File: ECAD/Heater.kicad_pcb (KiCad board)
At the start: 2 copper layers, 200 x 200 mm, 11 parts, among them J1 Conn_01x01_Female, J2 Conn_01x01_Female

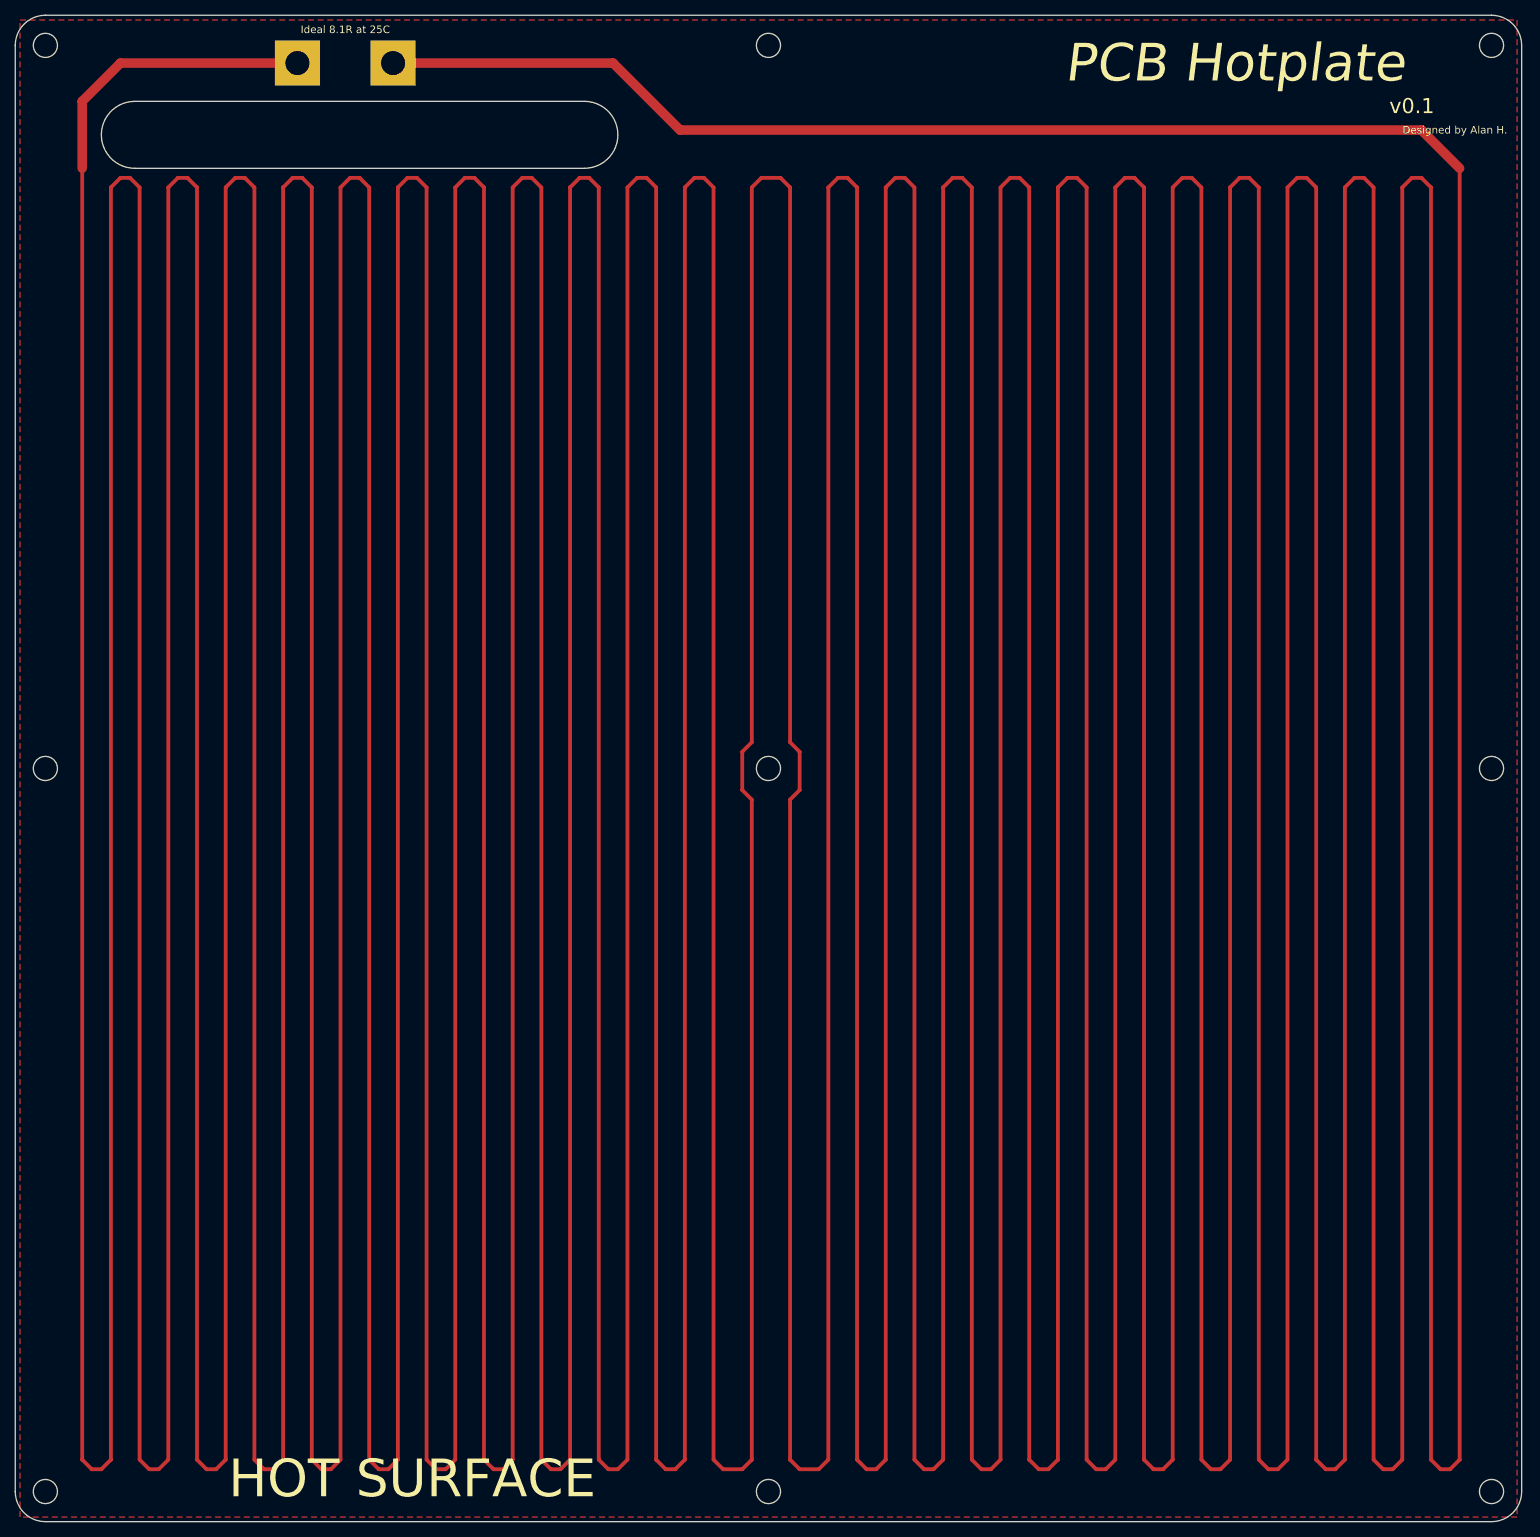
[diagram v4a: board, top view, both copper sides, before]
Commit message: Revert "Merge pull request #3 from Alan-JH/revert-2-Perforated-Heater"
This reverts commit 4dedab5329d0c4c589ebeff6f2ce44676f29a142, reversing
changes made to 18337d37710a704d8d57a7691b9b75f48685949f.
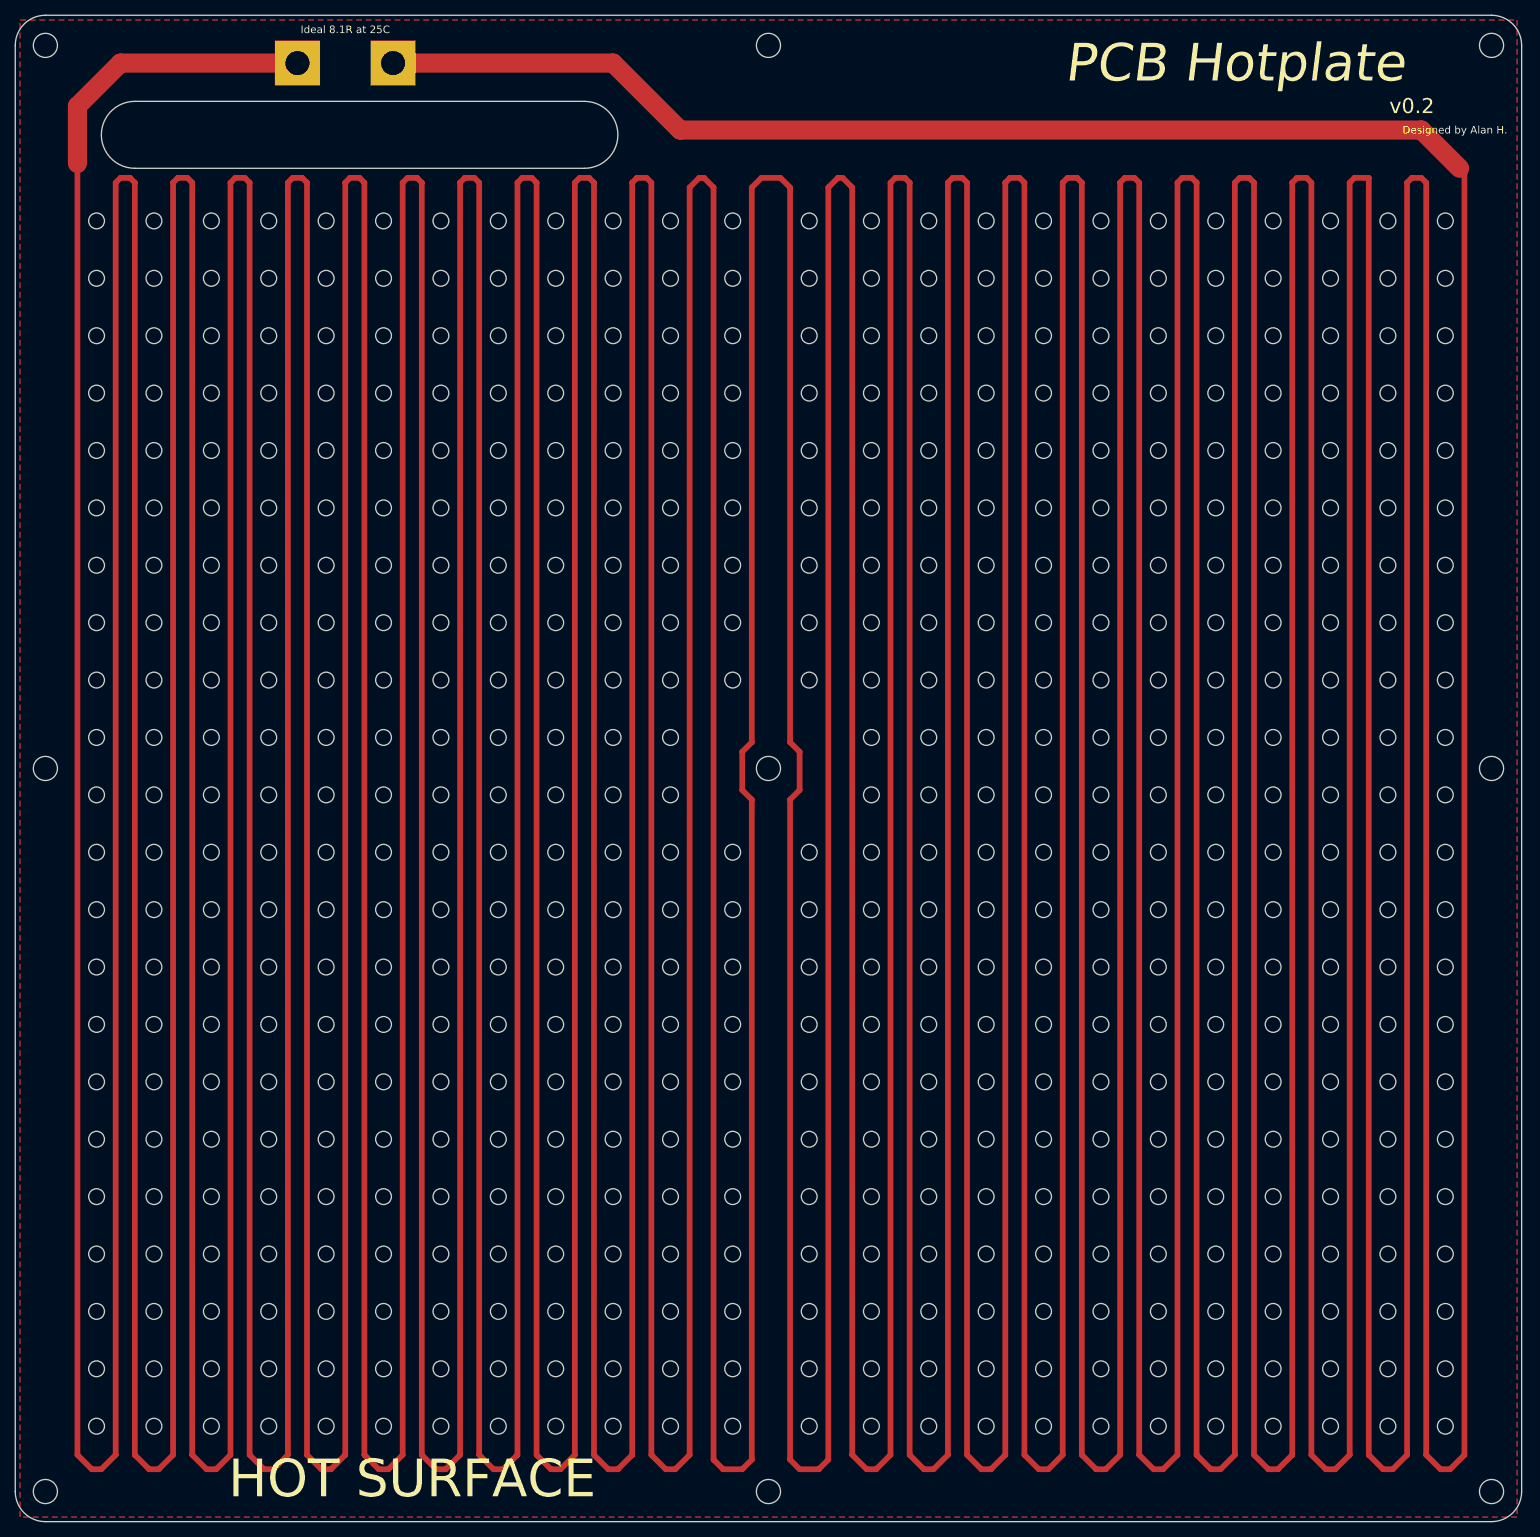
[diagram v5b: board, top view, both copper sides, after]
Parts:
- added REF**: MountingHole_2.1mm, MountingHole:MountingHole_2.1mm, F.Cu at (97.2, 37.5)
- added REF**: MountingHole_2.1mm, MountingHole:MountingHole_2.1mm, F.Cu at (81.9, 37.5)
- added REF**: MountingHole_2.1mm, MountingHole:MountingHole_2.1mm, F.Cu at (146.7, 67.9)
- added REF**: MountingHole_2.1mm, MountingHole:MountingHole_2.1mm, F.Cu at (89.5, 67.9)
- added REF**: MountingHole_2.1mm, MountingHole:MountingHole_2.1mm, F.Cu at (139.1, 67.9)
- added REF**: MountingHole_2.1mm, MountingHole:MountingHole_2.1mm, F.Cu at (123.8, 67.9)
- added REF**: MountingHole_2.1mm, MountingHole:MountingHole_2.1mm, F.Cu at (105.4, 67.9)
- added REF**: MountingHole_2.1mm, MountingHole:MountingHole_2.1mm, F.Cu at (115.6, 67.9)
- added REF**: MountingHole_2.1mm, MountingHole:MountingHole_2.1mm, F.Cu at (81.9, 67.9)
- added REF**: MountingHole_2.1mm, MountingHole:MountingHole_2.1mm, F.Cu at (74.3, 67.9)
- added REF**: MountingHole_2.1mm, MountingHole:MountingHole_2.1mm, F.Cu at (66.7, 67.9)
- added REF**: MountingHole_2.1mm, MountingHole:MountingHole_2.1mm, F.Cu at (51.4, 67.9)
- added REF**: MountingHole_2.1mm, MountingHole:MountingHole_2.1mm, F.Cu at (74.3, 37.5)
- added REF**: MountingHole_2.1mm, MountingHole:MountingHole_2.1mm, F.Cu at (59.1, 67.9)
- added REF**: MountingHole_2.1mm, MountingHole:MountingHole_2.1mm, F.Cu at (43.8, 67.9)
- added REF**: MountingHole_2.1mm, MountingHole:MountingHole_2.1mm, F.Cu at (28.6, 67.9)
- added REF**: MountingHole_2.1mm, MountingHole:MountingHole_2.1mm, F.Cu at (21.0, 67.9)
- added REF**: MountingHole_2.1mm, MountingHole:MountingHole_2.1mm, F.Cu at (200.0, 75.6)
- added REF**: MountingHole_2.1mm, MountingHole:MountingHole_2.1mm, F.Cu at (192.4, 75.6)
- added REF**: MountingHole_2.1mm, MountingHole:MountingHole_2.1mm, F.Cu at (184.8, 75.6)
- added REF**: MountingHole_2.1mm, MountingHole:MountingHole_2.1mm, F.Cu at (177.2, 75.6)
- added REF**: MountingHole_2.1mm, MountingHole:MountingHole_2.1mm, F.Cu at (169.5, 75.6)
- added REF**: MountingHole_2.1mm, MountingHole:MountingHole_2.1mm, F.Cu at (146.7, 75.6)
- added REF**: MountingHole_2.1mm, MountingHole:MountingHole_2.1mm, F.Cu at (66.7, 37.5)
- added REF**: MountingHole_2.1mm, MountingHole:MountingHole_2.1mm, F.Cu at (161.9, 75.6)
- added REF**: MountingHole_2.1mm, MountingHole:MountingHole_2.1mm, F.Cu at (154.3, 75.6)
- added REF**: MountingHole_2.1mm, MountingHole:MountingHole_2.1mm, F.Cu at (139.1, 75.6)
- added REF**: MountingHole_2.1mm, MountingHole:MountingHole_2.1mm, F.Cu at (131.4, 75.6)
- added REF**: MountingHole_2.1mm, MountingHole:MountingHole_2.1mm, F.Cu at (123.8, 75.6)
- added REF**: MountingHole_2.1mm, MountingHole:MountingHole_2.1mm, F.Cu at (115.6, 75.6)
- added REF**: MountingHole_2.1mm, MountingHole:MountingHole_2.1mm, F.Cu at (105.4, 75.6)
- added REF**: MountingHole_2.1mm, MountingHole:MountingHole_2.1mm, F.Cu at (97.2, 75.6)
- added REF**: MountingHole_2.1mm, MountingHole:MountingHole_2.1mm, F.Cu at (89.5, 75.6)
- added REF**: MountingHole_2.1mm, MountingHole:MountingHole_2.1mm, F.Cu at (51.4, 75.6)
- added REF**: MountingHole_2.1mm, MountingHole:MountingHole_2.1mm, F.Cu at (51.4, 37.5)
- added REF**: MountingHole_2.1mm, MountingHole:MountingHole_2.1mm, F.Cu at (43.8, 75.6)
- added REF**: MountingHole_2.1mm, MountingHole:MountingHole_2.1mm, F.Cu at (36.2, 75.6)
- added REF**: MountingHole_2.1mm, MountingHole:MountingHole_2.1mm, F.Cu at (36.2, 67.9)
- added REF**: MountingHole_2.1mm, MountingHole:MountingHole_2.1mm, F.Cu at (66.7, 75.6)
- added REF**: MountingHole_2.1mm, MountingHole:MountingHole_2.1mm, F.Cu at (81.9, 75.6)
- added REF**: MountingHole_2.1mm, MountingHole:MountingHole_2.1mm, F.Cu at (59.1, 75.6)
- added REF**: MountingHole_2.1mm, MountingHole:MountingHole_2.1mm, F.Cu at (74.3, 75.6)
- added REF**: MountingHole_2.1mm, MountingHole:MountingHole_2.1mm, F.Cu at (28.6, 75.6)
- added REF**: MountingHole_2.1mm, MountingHole:MountingHole_2.1mm, F.Cu at (21.0, 75.6)
- added REF**: MountingHole_2.1mm, MountingHole:MountingHole_2.1mm, F.Cu at (192.4, 67.9)
- added REF**: MountingHole_2.1mm, MountingHole:MountingHole_2.1mm, F.Cu at (59.1, 37.5)
- added REF**: MountingHole_2.1mm, MountingHole:MountingHole_2.1mm, F.Cu at (161.9, 67.9)
- added REF**: MountingHole_2.1mm, MountingHole:MountingHole_2.1mm, F.Cu at (169.5, 67.9)
- added REF**: MountingHole_2.1mm, MountingHole:MountingHole_2.1mm, F.Cu at (184.8, 67.9)
- added REF**: MountingHole_2.1mm, MountingHole:MountingHole_2.1mm, F.Cu at (200.0, 67.9)
- added REF**: MountingHole_2.1mm, MountingHole:MountingHole_2.1mm, F.Cu at (177.2, 67.9)
- added REF**: MountingHole_2.1mm, MountingHole:MountingHole_2.1mm, F.Cu at (97.2, 83.2)
- added REF**: MountingHole_2.1mm, MountingHole:MountingHole_2.1mm, F.Cu at (131.4, 83.2)
- added REF**: MountingHole_2.1mm, MountingHole:MountingHole_2.1mm, F.Cu at (154.3, 83.2)
- added REF**: MountingHole_2.1mm, MountingHole:MountingHole_2.1mm, F.Cu at (146.7, 83.2)
- added REF**: MountingHole_2.1mm, MountingHole:MountingHole_2.1mm, F.Cu at (89.5, 83.2)
- added REF**: MountingHole_2.1mm, MountingHole:MountingHole_2.1mm, F.Cu at (43.8, 37.5)
- added REF**: MountingHole_2.1mm, MountingHole:MountingHole_2.1mm, F.Cu at (139.1, 83.2)
- added REF**: MountingHole_2.1mm, MountingHole:MountingHole_2.1mm, F.Cu at (123.8, 83.2)
- added REF**: MountingHole_2.1mm, MountingHole:MountingHole_2.1mm, F.Cu at (105.4, 83.2)
- added REF**: MountingHole_2.1mm, MountingHole:MountingHole_2.1mm, F.Cu at (115.6, 83.2)
- added REF**: MountingHole_2.1mm, MountingHole:MountingHole_2.1mm, F.Cu at (81.9, 83.2)
- added REF**: MountingHole_2.1mm, MountingHole:MountingHole_2.1mm, F.Cu at (74.3, 83.2)
- added REF**: MountingHole_2.1mm, MountingHole:MountingHole_2.1mm, F.Cu at (66.7, 83.2)
- added REF**: MountingHole_2.1mm, MountingHole:MountingHole_2.1mm, F.Cu at (51.4, 83.2)
- added REF**: MountingHole_2.1mm, MountingHole:MountingHole_2.1mm, F.Cu at (59.1, 83.2)
- added REF**: MountingHole_2.1mm, MountingHole:MountingHole_2.1mm, F.Cu at (43.8, 83.2)
- added REF**: MountingHole_2.1mm, MountingHole:MountingHole_2.1mm, F.Cu at (28.6, 37.5)
- added REF**: MountingHole_2.1mm, MountingHole:MountingHole_2.1mm, F.Cu at (28.6, 83.2)
- added REF**: MountingHole_2.1mm, MountingHole:MountingHole_2.1mm, F.Cu at (21.0, 83.2)
- added REF**: MountingHole_2.1mm, MountingHole:MountingHole_2.1mm, F.Cu at (200.0, 90.8)
- added REF**: MountingHole_2.1mm, MountingHole:MountingHole_2.1mm, F.Cu at (192.4, 90.8)
- added REF**: MountingHole_2.1mm, MountingHole:MountingHole_2.1mm, F.Cu at (184.8, 90.8)
- added REF**: MountingHole_2.1mm, MountingHole:MountingHole_2.1mm, F.Cu at (177.2, 90.8)
- added REF**: MountingHole_2.1mm, MountingHole:MountingHole_2.1mm, F.Cu at (169.5, 90.8)
- added REF**: MountingHole_2.1mm, MountingHole:MountingHole_2.1mm, F.Cu at (146.7, 90.8)
- added REF**: MountingHole_2.1mm, MountingHole:MountingHole_2.1mm, F.Cu at (161.9, 90.8)
- added REF**: MountingHole_2.1mm, MountingHole:MountingHole_2.1mm, F.Cu at (154.3, 90.8)
- added REF**: MountingHole_2.1mm, MountingHole:MountingHole_2.1mm, F.Cu at (21.0, 37.5)
- added REF**: MountingHole_2.1mm, MountingHole:MountingHole_2.1mm, F.Cu at (139.1, 90.8)
- added REF**: MountingHole_2.1mm, MountingHole:MountingHole_2.1mm, F.Cu at (131.4, 90.8)
- added REF**: MountingHole_2.1mm, MountingHole:MountingHole_2.1mm, F.Cu at (123.8, 90.8)
- added REF**: MountingHole_2.1mm, MountingHole:MountingHole_2.1mm, F.Cu at (115.6, 90.8)
- added REF**: MountingHole_2.1mm, MountingHole:MountingHole_2.1mm, F.Cu at (105.4, 90.8)
- added REF**: MountingHole_2.1mm, MountingHole:MountingHole_2.1mm, F.Cu at (97.2, 90.8)
- added REF**: MountingHole_2.1mm, MountingHole:MountingHole_2.1mm, F.Cu at (89.5, 90.8)
- added REF**: MountingHole_2.1mm, MountingHole:MountingHole_2.1mm, F.Cu at (51.4, 90.8)
- added REF**: MountingHole_2.1mm, MountingHole:MountingHole_2.1mm, F.Cu at (43.8, 90.8)
- added REF**: MountingHole_2.1mm, MountingHole:MountingHole_2.1mm, F.Cu at (36.2, 90.8)
- added REF**: MountingHole_2.1mm, MountingHole:MountingHole_2.1mm, F.Cu at (200.0, 45.1)
- added REF**: MountingHole_2.1mm, MountingHole:MountingHole_2.1mm, F.Cu at (36.2, 83.2)
- added REF**: MountingHole_2.1mm, MountingHole:MountingHole_2.1mm, F.Cu at (66.7, 90.8)
- added REF**: MountingHole_2.1mm, MountingHole:MountingHole_2.1mm, F.Cu at (81.9, 90.8)
- added REF**: MountingHole_2.1mm, MountingHole:MountingHole_2.1mm, F.Cu at (59.1, 90.8)
- added REF**: MountingHole_2.1mm, MountingHole:MountingHole_2.1mm, F.Cu at (74.3, 90.8)
- added REF**: MountingHole_2.1mm, MountingHole:MountingHole_2.1mm, F.Cu at (28.6, 90.8)
- added REF**: MountingHole_2.1mm, MountingHole:MountingHole_2.1mm, F.Cu at (21.0, 90.8)
- added REF**: MountingHole_2.1mm, MountingHole:MountingHole_2.1mm, F.Cu at (192.4, 83.2)
- added REF**: MountingHole_2.1mm, MountingHole:MountingHole_2.1mm, F.Cu at (161.9, 83.2)
- added REF**: MountingHole_2.1mm, MountingHole:MountingHole_2.1mm, F.Cu at (169.5, 83.2)
- added REF**: MountingHole_2.1mm, MountingHole:MountingHole_2.1mm, F.Cu at (192.4, 45.1)
- added REF**: MountingHole_2.1mm, MountingHole:MountingHole_2.1mm, F.Cu at (184.8, 83.2)
- added REF**: MountingHole_2.1mm, MountingHole:MountingHole_2.1mm, F.Cu at (200.0, 83.2)
- added REF**: MountingHole_2.1mm, MountingHole:MountingHole_2.1mm, F.Cu at (177.2, 83.2)
- added REF**: MountingHole_2.1mm, MountingHole:MountingHole_2.1mm, F.Cu at (97.2, 98.4)
- added REF**: MountingHole_2.1mm, MountingHole:MountingHole_2.1mm, F.Cu at (131.4, 98.4)
- added REF**: MountingHole_2.1mm, MountingHole:MountingHole_2.1mm, F.Cu at (154.3, 98.4)
- added REF**: MountingHole_2.1mm, MountingHole:MountingHole_2.1mm, F.Cu at (146.7, 98.4)
- added REF**: MountingHole_2.1mm, MountingHole:MountingHole_2.1mm, F.Cu at (89.5, 98.4)
- added REF**: MountingHole_2.1mm, MountingHole:MountingHole_2.1mm, F.Cu at (139.1, 98.4)
- added REF**: MountingHole_2.1mm, MountingHole:MountingHole_2.1mm, F.Cu at (123.8, 98.4)
- added REF**: MountingHole_2.1mm, MountingHole:MountingHole_2.1mm, F.Cu at (131.4, 37.5)
- added REF**: MountingHole_2.1mm, MountingHole:MountingHole_2.1mm, F.Cu at (184.8, 45.1)
- added REF**: MountingHole_2.1mm, MountingHole:MountingHole_2.1mm, F.Cu at (105.4, 98.4)
- added REF**: MountingHole_2.1mm, MountingHole:MountingHole_2.1mm, F.Cu at (115.6, 98.4)
- added REF**: MountingHole_2.1mm, MountingHole:MountingHole_2.1mm, F.Cu at (81.9, 98.4)
- added REF**: MountingHole_2.1mm, MountingHole:MountingHole_2.1mm, F.Cu at (74.3, 98.4)
- added REF**: MountingHole_2.1mm, MountingHole:MountingHole_2.1mm, F.Cu at (66.7, 98.4)
- added REF**: MountingHole_2.1mm, MountingHole:MountingHole_2.1mm, F.Cu at (51.4, 98.4)
- added REF**: MountingHole_2.1mm, MountingHole:MountingHole_2.1mm, F.Cu at (59.1, 98.4)
- added REF**: MountingHole_2.1mm, MountingHole:MountingHole_2.1mm, F.Cu at (43.8, 98.4)
- added REF**: MountingHole_2.1mm, MountingHole:MountingHole_2.1mm, F.Cu at (28.6, 98.4)
- added REF**: MountingHole_2.1mm, MountingHole:MountingHole_2.1mm, F.Cu at (21.0, 98.4)
- added REF**: MountingHole_2.1mm, MountingHole:MountingHole_2.1mm, F.Cu at (177.2, 45.1)
- added REF**: MountingHole_2.1mm, MountingHole:MountingHole_2.1mm, F.Cu at (200.0, 106.0)
- added REF**: MountingHole_2.1mm, MountingHole:MountingHole_2.1mm, F.Cu at (192.4, 106.0)
- added REF**: MountingHole_2.1mm, MountingHole:MountingHole_2.1mm, F.Cu at (184.8, 106.0)
- added REF**: MountingHole_2.1mm, MountingHole:MountingHole_2.1mm, F.Cu at (177.2, 106.0)
- added REF**: MountingHole_2.1mm, MountingHole:MountingHole_2.1mm, F.Cu at (169.5, 106.0)
- added REF**: MountingHole_2.1mm, MountingHole:MountingHole_2.1mm, F.Cu at (146.7, 106.0)
- added REF**: MountingHole_2.1mm, MountingHole:MountingHole_2.1mm, F.Cu at (161.9, 106.0)
- added REF**: MountingHole_2.1mm, MountingHole:MountingHole_2.1mm, F.Cu at (154.3, 106.0)
- added REF**: MountingHole_2.1mm, MountingHole:MountingHole_2.1mm, F.Cu at (139.1, 106.0)
- added REF**: MountingHole_2.1mm, MountingHole:MountingHole_2.1mm, F.Cu at (131.4, 106.0)
- added REF**: MountingHole_2.1mm, MountingHole:MountingHole_2.1mm, F.Cu at (169.5, 45.1)
- added REF**: MountingHole_2.1mm, MountingHole:MountingHole_2.1mm, F.Cu at (123.8, 106.0)
- added REF**: MountingHole_2.1mm, MountingHole:MountingHole_2.1mm, F.Cu at (97.2, 106.0)
- added REF**: MountingHole_2.1mm, MountingHole:MountingHole_2.1mm, F.Cu at (89.5, 106.0)
- added REF**: MountingHole_2.1mm, MountingHole:MountingHole_2.1mm, F.Cu at (51.4, 106.0)
- added REF**: MountingHole_2.1mm, MountingHole:MountingHole_2.1mm, F.Cu at (43.8, 106.0)
- added REF**: MountingHole_2.1mm, MountingHole:MountingHole_2.1mm, F.Cu at (36.2, 106.0)
- added REF**: MountingHole_2.1mm, MountingHole:MountingHole_2.1mm, F.Cu at (36.2, 98.4)
- added REF**: MountingHole_2.1mm, MountingHole:MountingHole_2.1mm, F.Cu at (66.7, 106.0)
- added REF**: MountingHole_2.1mm, MountingHole:MountingHole_2.1mm, F.Cu at (81.9, 106.0)
- added REF**: MountingHole_2.1mm, MountingHole:MountingHole_2.1mm, F.Cu at (59.1, 106.0)
- added REF**: MountingHole_2.1mm, MountingHole:MountingHole_2.1mm, F.Cu at (146.7, 45.1)
- added REF**: MountingHole_2.1mm, MountingHole:MountingHole_2.1mm, F.Cu at (74.3, 106.0)
- added REF**: MountingHole_2.1mm, MountingHole:MountingHole_2.1mm, F.Cu at (28.6, 106.0)
- added REF**: MountingHole_2.1mm, MountingHole:MountingHole_2.1mm, F.Cu at (21.0, 106.0)
- added REF**: MountingHole_2.1mm, MountingHole:MountingHole_2.1mm, F.Cu at (192.4, 98.4)
- added REF**: MountingHole_2.1mm, MountingHole:MountingHole_2.1mm, F.Cu at (161.9, 98.4)
- added REF**: MountingHole_2.1mm, MountingHole:MountingHole_2.1mm, F.Cu at (169.5, 98.4)
- added REF**: MountingHole_2.1mm, MountingHole:MountingHole_2.1mm, F.Cu at (184.8, 98.4)
- added REF**: MountingHole_2.1mm, MountingHole:MountingHole_2.1mm, F.Cu at (200.0, 98.4)
- added REF**: MountingHole_2.1mm, MountingHole:MountingHole_2.1mm, F.Cu at (177.2, 98.4)
- added REF**: MountingHole_2.1mm, MountingHole:MountingHole_2.1mm, F.Cu at (97.2, 113.7)
- added REF**: MountingHole_2.1mm, MountingHole:MountingHole_2.1mm, F.Cu at (161.9, 45.1)
- added REF**: MountingHole_2.1mm, MountingHole:MountingHole_2.1mm, F.Cu at (131.4, 113.7)
- added REF**: MountingHole_2.1mm, MountingHole:MountingHole_2.1mm, F.Cu at (154.3, 113.7)
- added REF**: MountingHole_2.1mm, MountingHole:MountingHole_2.1mm, F.Cu at (146.7, 113.7)
- added REF**: MountingHole_2.1mm, MountingHole:MountingHole_2.1mm, F.Cu at (89.5, 113.7)
- added REF**: MountingHole_2.1mm, MountingHole:MountingHole_2.1mm, F.Cu at (139.1, 113.7)
- added REF**: MountingHole_2.1mm, MountingHole:MountingHole_2.1mm, F.Cu at (123.8, 113.7)
- added REF**: MountingHole_2.1mm, MountingHole:MountingHole_2.1mm, F.Cu at (81.9, 113.7)
- added REF**: MountingHole_2.1mm, MountingHole:MountingHole_2.1mm, F.Cu at (74.3, 113.7)
- added REF**: MountingHole_2.1mm, MountingHole:MountingHole_2.1mm, F.Cu at (66.7, 113.7)
- added REF**: MountingHole_2.1mm, MountingHole:MountingHole_2.1mm, F.Cu at (51.4, 113.7)
- added REF**: MountingHole_2.1mm, MountingHole:MountingHole_2.1mm, F.Cu at (154.3, 45.1)
- added REF**: MountingHole_2.1mm, MountingHole:MountingHole_2.1mm, F.Cu at (59.1, 113.7)
- added REF**: MountingHole_2.1mm, MountingHole:MountingHole_2.1mm, F.Cu at (43.8, 113.7)
- added REF**: MountingHole_2.1mm, MountingHole:MountingHole_2.1mm, F.Cu at (28.6, 113.7)
- added REF**: MountingHole_2.1mm, MountingHole:MountingHole_2.1mm, F.Cu at (21.0, 113.7)
- added REF**: MountingHole_2.1mm, MountingHole:MountingHole_2.1mm, F.Cu at (200.0, 121.3)
- added REF**: MountingHole_2.1mm, MountingHole:MountingHole_2.1mm, F.Cu at (192.4, 121.3)
- added REF**: MountingHole_2.1mm, MountingHole:MountingHole_2.1mm, F.Cu at (184.8, 121.3)
- added REF**: MountingHole_2.1mm, MountingHole:MountingHole_2.1mm, F.Cu at (177.2, 121.3)
- added REF**: MountingHole_2.1mm, MountingHole:MountingHole_2.1mm, F.Cu at (169.5, 121.3)
- added REF**: MountingHole_2.1mm, MountingHole:MountingHole_2.1mm, F.Cu at (146.7, 121.3)
- added REF**: MountingHole_2.1mm, MountingHole:MountingHole_2.1mm, F.Cu at (139.1, 45.1)
- added REF**: MountingHole_2.1mm, MountingHole:MountingHole_2.1mm, F.Cu at (161.9, 121.3)
- added REF**: MountingHole_2.1mm, MountingHole:MountingHole_2.1mm, F.Cu at (154.3, 121.3)
- added REF**: MountingHole_2.1mm, MountingHole:MountingHole_2.1mm, F.Cu at (139.1, 121.3)
- added REF**: MountingHole_2.1mm, MountingHole:MountingHole_2.1mm, F.Cu at (131.4, 121.3)
- added REF**: MountingHole_2.1mm, MountingHole:MountingHole_2.1mm, F.Cu at (123.8, 121.3)
- added REF**: MountingHole_2.1mm, MountingHole:MountingHole_2.1mm, F.Cu at (115.6, 121.3)
- added REF**: MountingHole_2.1mm, MountingHole:MountingHole_2.1mm, F.Cu at (105.4, 121.3)
- added REF**: MountingHole_2.1mm, MountingHole:MountingHole_2.1mm, F.Cu at (97.2, 121.3)
- added REF**: MountingHole_2.1mm, MountingHole:MountingHole_2.1mm, F.Cu at (89.5, 121.3)
- added REF**: MountingHole_2.1mm, MountingHole:MountingHole_2.1mm, F.Cu at (51.4, 121.3)
- added REF**: MountingHole_2.1mm, MountingHole:MountingHole_2.1mm, F.Cu at (131.4, 45.1)
- added REF**: MountingHole_2.1mm, MountingHole:MountingHole_2.1mm, F.Cu at (43.8, 121.3)
- added REF**: MountingHole_2.1mm, MountingHole:MountingHole_2.1mm, F.Cu at (36.2, 121.3)
- added REF**: MountingHole_2.1mm, MountingHole:MountingHole_2.1mm, F.Cu at (36.2, 113.7)
- added REF**: MountingHole_2.1mm, MountingHole:MountingHole_2.1mm, F.Cu at (66.7, 121.3)
- added REF**: MountingHole_2.1mm, MountingHole:MountingHole_2.1mm, F.Cu at (81.9, 121.3)
- added REF**: MountingHole_2.1mm, MountingHole:MountingHole_2.1mm, F.Cu at (59.1, 121.3)
- added REF**: MountingHole_2.1mm, MountingHole:MountingHole_2.1mm, F.Cu at (74.3, 121.3)
- added REF**: MountingHole_2.1mm, MountingHole:MountingHole_2.1mm, F.Cu at (28.6, 121.3)
- added REF**: MountingHole_2.1mm, MountingHole:MountingHole_2.1mm, F.Cu at (21.0, 121.3)
- added REF**: MountingHole_2.1mm, MountingHole:MountingHole_2.1mm, F.Cu at (192.4, 113.7)
- added REF**: MountingHole_2.1mm, MountingHole:MountingHole_2.1mm, F.Cu at (123.8, 45.1)
- added REF**: MountingHole_2.1mm, MountingHole:MountingHole_2.1mm, F.Cu at (161.9, 113.7)
- added REF**: MountingHole_2.1mm, MountingHole:MountingHole_2.1mm, F.Cu at (169.5, 113.7)
- added REF**: MountingHole_2.1mm, MountingHole:MountingHole_2.1mm, F.Cu at (184.8, 113.7)
- added REF**: MountingHole_2.1mm, MountingHole:MountingHole_2.1mm, F.Cu at (200.0, 113.7)
- added REF**: MountingHole_2.1mm, MountingHole:MountingHole_2.1mm, F.Cu at (177.2, 113.7)
- added REF**: MountingHole_2.1mm, MountingHole:MountingHole_2.1mm, F.Cu at (97.2, 128.9)
- added REF**: MountingHole_2.1mm, MountingHole:MountingHole_2.1mm, F.Cu at (131.4, 128.9)
- added REF**: MountingHole_2.1mm, MountingHole:MountingHole_2.1mm, F.Cu at (154.3, 128.9)
- added REF**: MountingHole_2.1mm, MountingHole:MountingHole_2.1mm, F.Cu at (146.7, 128.9)
- added REF**: MountingHole_2.1mm, MountingHole:MountingHole_2.1mm, F.Cu at (89.5, 128.9)
- added REF**: MountingHole_2.1mm, MountingHole:MountingHole_2.1mm, F.Cu at (115.6, 45.1)
- added REF**: MountingHole_2.1mm, MountingHole:MountingHole_2.1mm, F.Cu at (139.1, 128.9)
- added REF**: MountingHole_2.1mm, MountingHole:MountingHole_2.1mm, F.Cu at (123.8, 128.9)
- added REF**: MountingHole_2.1mm, MountingHole:MountingHole_2.1mm, F.Cu at (105.4, 128.9)
- added REF**: MountingHole_2.1mm, MountingHole:MountingHole_2.1mm, F.Cu at (115.6, 128.9)
- added REF**: MountingHole_2.1mm, MountingHole:MountingHole_2.1mm, F.Cu at (81.9, 128.9)
- added REF**: MountingHole_2.1mm, MountingHole:MountingHole_2.1mm, F.Cu at (74.3, 128.9)
- added REF**: MountingHole_2.1mm, MountingHole:MountingHole_2.1mm, F.Cu at (66.7, 128.9)
- added REF**: MountingHole_2.1mm, MountingHole:MountingHole_2.1mm, F.Cu at (51.4, 128.9)
- added REF**: MountingHole_2.1mm, MountingHole:MountingHole_2.1mm, F.Cu at (59.1, 128.9)
- added REF**: MountingHole_2.1mm, MountingHole:MountingHole_2.1mm, F.Cu at (43.8, 128.9)
- added REF**: MountingHole_2.1mm, MountingHole:MountingHole_2.1mm, F.Cu at (154.3, 37.5)
- added REF**: MountingHole_2.1mm, MountingHole:MountingHole_2.1mm, F.Cu at (105.4, 45.1)
- added REF**: MountingHole_2.1mm, MountingHole:MountingHole_2.1mm, F.Cu at (28.6, 128.9)
- added REF**: MountingHole_2.1mm, MountingHole:MountingHole_2.1mm, F.Cu at (21.0, 128.9)
- added REF**: MountingHole_2.1mm, MountingHole:MountingHole_2.1mm, F.Cu at (200.0, 136.5)
- added REF**: MountingHole_2.1mm, MountingHole:MountingHole_2.1mm, F.Cu at (192.4, 136.5)
- added REF**: MountingHole_2.1mm, MountingHole:MountingHole_2.1mm, F.Cu at (184.8, 136.5)
- added REF**: MountingHole_2.1mm, MountingHole:MountingHole_2.1mm, F.Cu at (177.2, 136.5)
- added REF**: MountingHole_2.1mm, MountingHole:MountingHole_2.1mm, F.Cu at (169.5, 136.5)
- added REF**: MountingHole_2.1mm, MountingHole:MountingHole_2.1mm, F.Cu at (146.7, 136.5)
- added REF**: MountingHole_2.1mm, MountingHole:MountingHole_2.1mm, F.Cu at (161.9, 136.5)
- added REF**: MountingHole_2.1mm, MountingHole:MountingHole_2.1mm, F.Cu at (154.3, 136.5)
- added REF**: MountingHole_2.1mm, MountingHole:MountingHole_2.1mm, F.Cu at (97.2, 45.1)
- added REF**: MountingHole_2.1mm, MountingHole:MountingHole_2.1mm, F.Cu at (139.1, 136.5)
- added REF**: MountingHole_2.1mm, MountingHole:MountingHole_2.1mm, F.Cu at (131.4, 136.5)
- added REF**: MountingHole_2.1mm, MountingHole:MountingHole_2.1mm, F.Cu at (123.8, 136.5)
- added REF**: MountingHole_2.1mm, MountingHole:MountingHole_2.1mm, F.Cu at (115.6, 136.5)
- added REF**: MountingHole_2.1mm, MountingHole:MountingHole_2.1mm, F.Cu at (105.4, 136.5)
- added REF**: MountingHole_2.1mm, MountingHole:MountingHole_2.1mm, F.Cu at (97.2, 136.5)
- added REF**: MountingHole_2.1mm, MountingHole:MountingHole_2.1mm, F.Cu at (89.5, 136.5)
- added REF**: MountingHole_2.1mm, MountingHole:MountingHole_2.1mm, F.Cu at (51.4, 136.5)
- added REF**: MountingHole_2.1mm, MountingHole:MountingHole_2.1mm, F.Cu at (43.8, 136.5)
- added REF**: MountingHole_2.1mm, MountingHole:MountingHole_2.1mm, F.Cu at (36.2, 136.5)
- added REF**: MountingHole_2.1mm, MountingHole:MountingHole_2.1mm, F.Cu at (89.5, 45.1)
- added REF**: MountingHole_2.1mm, MountingHole:MountingHole_2.1mm, F.Cu at (36.2, 128.9)
- added REF**: MountingHole_2.1mm, MountingHole:MountingHole_2.1mm, F.Cu at (66.7, 136.5)
- added REF**: MountingHole_2.1mm, MountingHole:MountingHole_2.1mm, F.Cu at (81.9, 136.5)
- added REF**: MountingHole_2.1mm, MountingHole:MountingHole_2.1mm, F.Cu at (59.1, 136.5)
- added REF**: MountingHole_2.1mm, MountingHole:MountingHole_2.1mm, F.Cu at (74.3, 136.5)
- added REF**: MountingHole_2.1mm, MountingHole:MountingHole_2.1mm, F.Cu at (28.6, 136.5)
- added REF**: MountingHole_2.1mm, MountingHole:MountingHole_2.1mm, F.Cu at (21.0, 136.5)
- added REF**: MountingHole_2.1mm, MountingHole:MountingHole_2.1mm, F.Cu at (192.4, 128.9)
- added REF**: MountingHole_2.1mm, MountingHole:MountingHole_2.1mm, F.Cu at (161.9, 128.9)
- added REF**: MountingHole_2.1mm, MountingHole:MountingHole_2.1mm, F.Cu at (169.5, 128.9)
- added REF**: MountingHole_2.1mm, MountingHole:MountingHole_2.1mm, F.Cu at (51.4, 45.1)
- added REF**: MountingHole_2.1mm, MountingHole:MountingHole_2.1mm, F.Cu at (184.8, 128.9)
- added REF**: MountingHole_2.1mm, MountingHole:MountingHole_2.1mm, F.Cu at (200.0, 128.9)
- added REF**: MountingHole_2.1mm, MountingHole:MountingHole_2.1mm, F.Cu at (177.2, 128.9)
- added REF**: MountingHole_2.1mm, MountingHole:MountingHole_2.1mm, F.Cu at (97.2, 144.1)
- added REF**: MountingHole_2.1mm, MountingHole:MountingHole_2.1mm, F.Cu at (131.4, 144.1)
- added REF**: MountingHole_2.1mm, MountingHole:MountingHole_2.1mm, F.Cu at (154.3, 144.1)
- added REF**: MountingHole_2.1mm, MountingHole:MountingHole_2.1mm, F.Cu at (146.7, 144.1)
- added REF**: MountingHole_2.1mm, MountingHole:MountingHole_2.1mm, F.Cu at (89.5, 144.1)
- added REF**: MountingHole_2.1mm, MountingHole:MountingHole_2.1mm, F.Cu at (139.1, 144.1)
- added REF**: MountingHole_2.1mm, MountingHole:MountingHole_2.1mm, F.Cu at (123.8, 144.1)
- added REF**: MountingHole_2.1mm, MountingHole:MountingHole_2.1mm, F.Cu at (43.8, 45.1)
- added REF**: MountingHole_2.1mm, MountingHole:MountingHole_2.1mm, F.Cu at (105.4, 144.1)
- added REF**: MountingHole_2.1mm, MountingHole:MountingHole_2.1mm, F.Cu at (115.6, 144.1)
- added REF**: MountingHole_2.1mm, MountingHole:MountingHole_2.1mm, F.Cu at (81.9, 144.1)
- added REF**: MountingHole_2.1mm, MountingHole:MountingHole_2.1mm, F.Cu at (74.3, 144.1)
- added REF**: MountingHole_2.1mm, MountingHole:MountingHole_2.1mm, F.Cu at (66.7, 144.1)
- added REF**: MountingHole_2.1mm, MountingHole:MountingHole_2.1mm, F.Cu at (51.4, 144.1)
- added REF**: MountingHole_2.1mm, MountingHole:MountingHole_2.1mm, F.Cu at (59.1, 144.1)
- added REF**: MountingHole_2.1mm, MountingHole:MountingHole_2.1mm, F.Cu at (43.8, 144.1)
- added REF**: MountingHole_2.1mm, MountingHole:MountingHole_2.1mm, F.Cu at (28.6, 144.1)
- added REF**: MountingHole_2.1mm, MountingHole:MountingHole_2.1mm, F.Cu at (21.0, 144.1)
- added REF**: MountingHole_2.1mm, MountingHole:MountingHole_2.1mm, F.Cu at (36.2, 45.1)
- added REF**: MountingHole_2.1mm, MountingHole:MountingHole_2.1mm, F.Cu at (200.0, 151.8)
- added REF**: MountingHole_2.1mm, MountingHole:MountingHole_2.1mm, F.Cu at (192.4, 151.8)
- added REF**: MountingHole_2.1mm, MountingHole:MountingHole_2.1mm, F.Cu at (184.8, 151.8)
- added REF**: MountingHole_2.1mm, MountingHole:MountingHole_2.1mm, F.Cu at (177.2, 151.8)
- added REF**: MountingHole_2.1mm, MountingHole:MountingHole_2.1mm, F.Cu at (169.5, 151.8)
- added REF**: MountingHole_2.1mm, MountingHole:MountingHole_2.1mm, F.Cu at (146.7, 151.8)
- added REF**: MountingHole_2.1mm, MountingHole:MountingHole_2.1mm, F.Cu at (161.9, 151.8)
- added REF**: MountingHole_2.1mm, MountingHole:MountingHole_2.1mm, F.Cu at (154.3, 151.8)
- added REF**: MountingHole_2.1mm, MountingHole:MountingHole_2.1mm, F.Cu at (139.1, 151.8)
- added REF**: MountingHole_2.1mm, MountingHole:MountingHole_2.1mm, F.Cu at (131.4, 151.8)
- added REF**: MountingHole_2.1mm, MountingHole:MountingHole_2.1mm, F.Cu at (36.2, 37.5)
- added REF**: MountingHole_2.1mm, MountingHole:MountingHole_2.1mm, F.Cu at (123.8, 151.8)
- added REF**: MountingHole_2.1mm, MountingHole:MountingHole_2.1mm, F.Cu at (115.6, 151.8)
- added REF**: MountingHole_2.1mm, MountingHole:MountingHole_2.1mm, F.Cu at (105.4, 151.8)
- added REF**: MountingHole_2.1mm, MountingHole:MountingHole_2.1mm, F.Cu at (97.2, 151.8)
- added REF**: MountingHole_2.1mm, MountingHole:MountingHole_2.1mm, F.Cu at (89.5, 151.8)
- added REF**: MountingHole_2.1mm, MountingHole:MountingHole_2.1mm, F.Cu at (51.4, 151.8)
- added REF**: MountingHole_2.1mm, MountingHole:MountingHole_2.1mm, F.Cu at (43.8, 151.8)
- added REF**: MountingHole_2.1mm, MountingHole:MountingHole_2.1mm, F.Cu at (36.2, 151.8)
- added REF**: MountingHole_2.1mm, MountingHole:MountingHole_2.1mm, F.Cu at (36.2, 144.1)
- added REF**: MountingHole_2.1mm, MountingHole:MountingHole_2.1mm, F.Cu at (66.7, 151.8)
- added REF**: MountingHole_2.1mm, MountingHole:MountingHole_2.1mm, F.Cu at (66.7, 45.1)
- added REF**: MountingHole_2.1mm, MountingHole:MountingHole_2.1mm, F.Cu at (81.9, 151.8)
- added REF**: MountingHole_2.1mm, MountingHole:MountingHole_2.1mm, F.Cu at (59.1, 151.8)
- added REF**: MountingHole_2.1mm, MountingHole:MountingHole_2.1mm, F.Cu at (74.3, 151.8)
- added REF**: MountingHole_2.1mm, MountingHole:MountingHole_2.1mm, F.Cu at (28.6, 151.8)
- added REF**: MountingHole_2.1mm, MountingHole:MountingHole_2.1mm, F.Cu at (21.0, 151.8)
- added REF**: MountingHole_2.1mm, MountingHole:MountingHole_2.1mm, F.Cu at (192.4, 144.1)
- added REF**: MountingHole_2.1mm, MountingHole:MountingHole_2.1mm, F.Cu at (161.9, 144.1)
- added REF**: MountingHole_2.1mm, MountingHole:MountingHole_2.1mm, F.Cu at (169.5, 144.1)
- added REF**: MountingHole_2.1mm, MountingHole:MountingHole_2.1mm, F.Cu at (184.8, 144.1)
- added REF**: MountingHole_2.1mm, MountingHole:MountingHole_2.1mm, F.Cu at (200.0, 144.1)
- added REF**: MountingHole_2.1mm, MountingHole:MountingHole_2.1mm, F.Cu at (81.9, 45.1)
- added REF**: MountingHole_2.1mm, MountingHole:MountingHole_2.1mm, F.Cu at (177.2, 144.1)
- added REF**: MountingHole_2.1mm, MountingHole:MountingHole_2.1mm, F.Cu at (97.2, 159.4)
- added REF**: MountingHole_2.1mm, MountingHole:MountingHole_2.1mm, F.Cu at (131.4, 159.4)
- added REF**: MountingHole_2.1mm, MountingHole:MountingHole_2.1mm, F.Cu at (154.3, 159.4)
- added REF**: MountingHole_2.1mm, MountingHole:MountingHole_2.1mm, F.Cu at (146.7, 159.4)
- added REF**: MountingHole_2.1mm, MountingHole:MountingHole_2.1mm, F.Cu at (89.5, 159.4)
- added REF**: MountingHole_2.1mm, MountingHole:MountingHole_2.1mm, F.Cu at (139.1, 159.4)
- added REF**: MountingHole_2.1mm, MountingHole:MountingHole_2.1mm, F.Cu at (123.8, 159.4)
- added REF**: MountingHole_2.1mm, MountingHole:MountingHole_2.1mm, F.Cu at (105.4, 159.4)
- added REF**: MountingHole_2.1mm, MountingHole:MountingHole_2.1mm, F.Cu at (115.6, 159.4)
- added REF**: MountingHole_2.1mm, MountingHole:MountingHole_2.1mm, F.Cu at (59.1, 45.1)
- added REF**: MountingHole_2.1mm, MountingHole:MountingHole_2.1mm, F.Cu at (81.9, 159.4)
- added REF**: MountingHole_2.1mm, MountingHole:MountingHole_2.1mm, F.Cu at (74.3, 159.4)
- added REF**: MountingHole_2.1mm, MountingHole:MountingHole_2.1mm, F.Cu at (66.7, 159.4)
- added REF**: MountingHole_2.1mm, MountingHole:MountingHole_2.1mm, F.Cu at (51.4, 159.4)
- added REF**: MountingHole_2.1mm, MountingHole:MountingHole_2.1mm, F.Cu at (59.1, 159.4)
- added REF**: MountingHole_2.1mm, MountingHole:MountingHole_2.1mm, F.Cu at (43.8, 159.4)
- added REF**: MountingHole_2.1mm, MountingHole:MountingHole_2.1mm, F.Cu at (28.6, 159.4)
- added REF**: MountingHole_2.1mm, MountingHole:MountingHole_2.1mm, F.Cu at (21.0, 159.4)
- added REF**: MountingHole_2.1mm, MountingHole:MountingHole_2.1mm, F.Cu at (200.0, 167.0)
- added REF**: MountingHole_2.1mm, MountingHole:MountingHole_2.1mm, F.Cu at (192.4, 167.0)
- added REF**: MountingHole_2.1mm, MountingHole:MountingHole_2.1mm, F.Cu at (146.7, 37.5)
- added REF**: MountingHole_2.1mm, MountingHole:MountingHole_2.1mm, F.Cu at (74.3, 45.1)
- added REF**: MountingHole_2.1mm, MountingHole:MountingHole_2.1mm, F.Cu at (184.8, 167.0)
- added REF**: MountingHole_2.1mm, MountingHole:MountingHole_2.1mm, F.Cu at (177.2, 167.0)
- added REF**: MountingHole_2.1mm, MountingHole:MountingHole_2.1mm, F.Cu at (169.5, 167.0)
- added REF**: MountingHole_2.1mm, MountingHole:MountingHole_2.1mm, F.Cu at (146.7, 167.0)
- added REF**: MountingHole_2.1mm, MountingHole:MountingHole_2.1mm, F.Cu at (161.9, 167.0)
- added REF**: MountingHole_2.1mm, MountingHole:MountingHole_2.1mm, F.Cu at (154.3, 167.0)
- added REF**: MountingHole_2.1mm, MountingHole:MountingHole_2.1mm, F.Cu at (139.1, 167.0)
- added REF**: MountingHole_2.1mm, MountingHole:MountingHole_2.1mm, F.Cu at (131.4, 167.0)
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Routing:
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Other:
- board text added: "v0.2"
- board text removed: "v0.1"

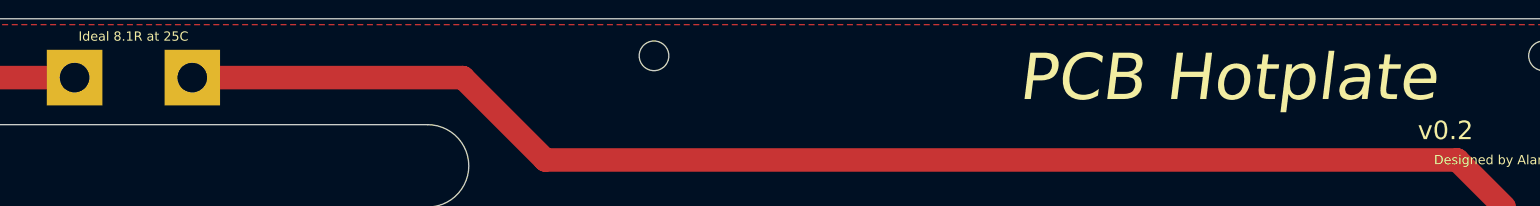
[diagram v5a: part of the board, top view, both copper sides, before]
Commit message: Update heater silkscreen info
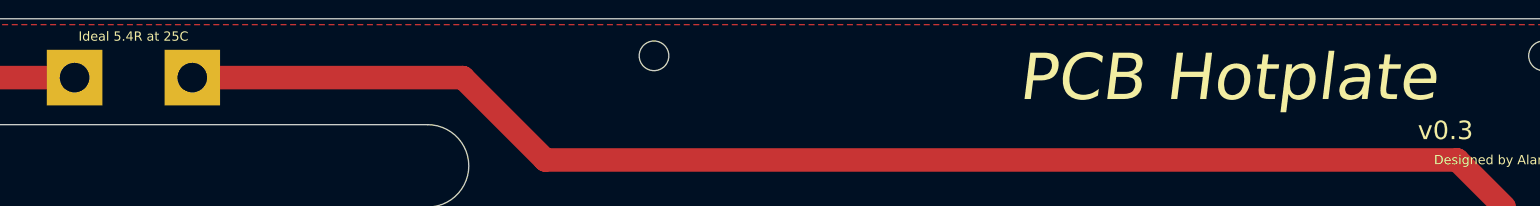
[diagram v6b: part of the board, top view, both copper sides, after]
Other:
- board text added: "Ideal 5.4R at 25C"
- board text added: "v0.3"
- board text removed: "Ideal 8.1R at 25C"
- board text removed: "v0.2"
